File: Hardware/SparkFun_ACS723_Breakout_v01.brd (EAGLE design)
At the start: 24.1 x 15.2 mm, 19 parts, among them U1 ACS723

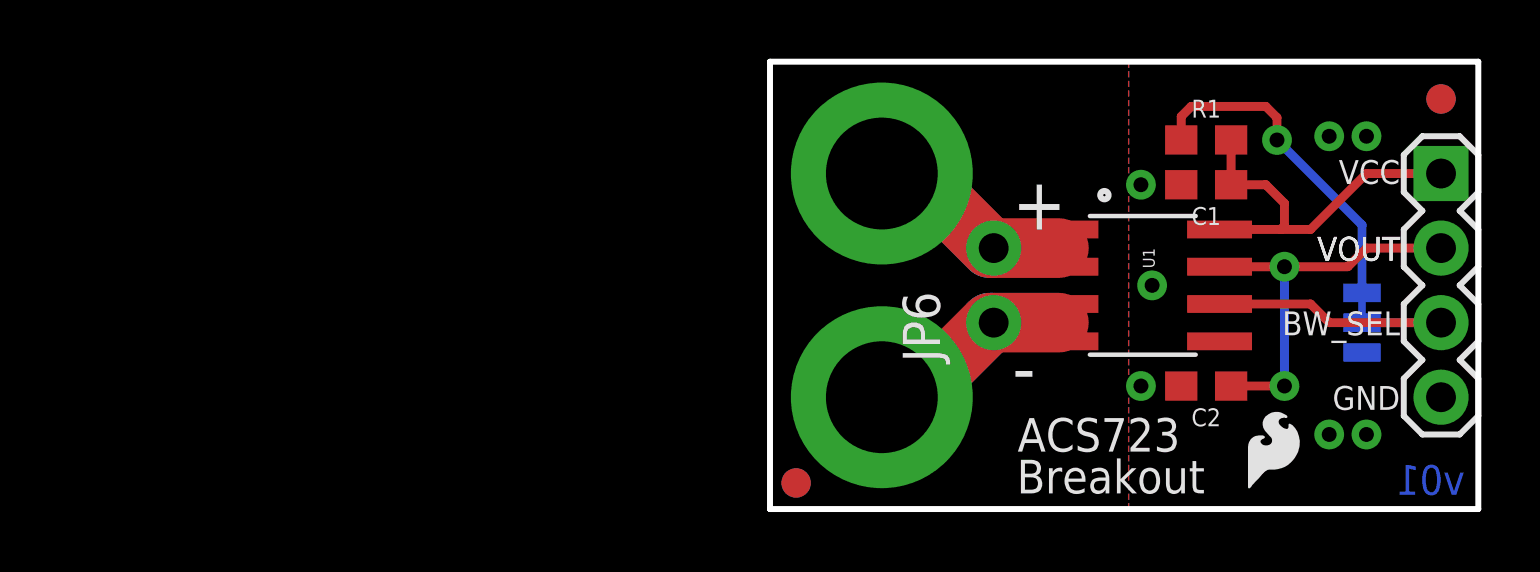
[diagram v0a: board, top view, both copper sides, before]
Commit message: finalizing v01 design
-isolated GND plane
-added 1nf decoupling cap to viout
-updated to 0603 footprints
-added bandwidth select jumper
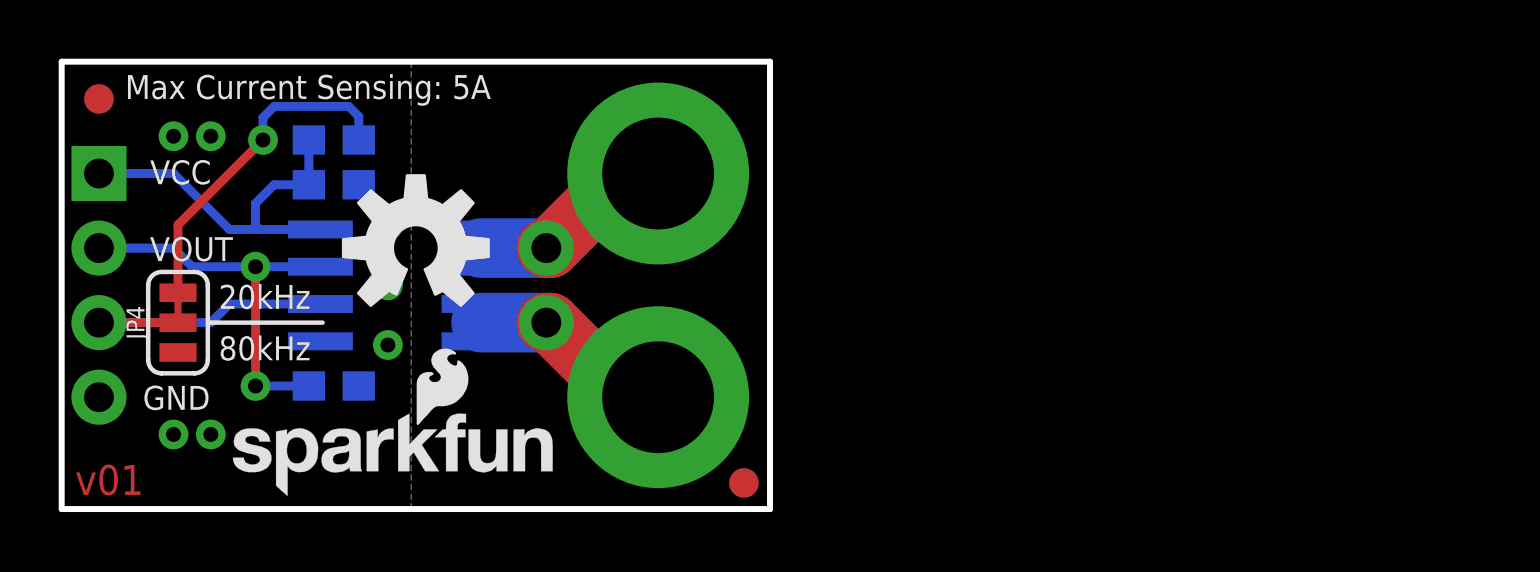
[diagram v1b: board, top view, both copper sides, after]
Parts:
- moved FD3 45.7 mm to (-22.9, 14.0), flipped to the top
- moved FD4 45.7 mm to (-22.9, 14.0), flipped to the bottom
- moved JP3 45.7 mm to (-22.9, 11.4), flipped to the bottom
- moved JP4 40.3 mm to (-20.2, 6.35), flipped to the top
- moved LOGO2 37.6 mm to (-18.8, -0.05), flipped to the top
- moved FRAME1 33.1 mm to (16.5, -11.4), flipped to the bottom
- moved U$6 32.0 mm to (-16.0, 0.38), flipped to the bottom
- moved C1 29.7 mm to (-14.9, 11.0), flipped to the bottom
- moved C2 29.7 mm to (-14.9, 4.19), flipped to the bottom
- moved R1 29.7 mm to (-14.9, 12.6), flipped to the bottom
- moved U1 25.4 mm to (-12.7, 7.62), flipped to the bottom
- moved U$5 24.6 mm to (-12.3, 2.54), flipped to the top
- moved U$3 24.1 mm to (-12.1, 8.89), flipped to the top
- moved JP6 15.2 mm to (-7.62, 6.35), flipped to the bottom
- moved U$1 10.2 mm to (5.08, -14.0), flipped to the bottom
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
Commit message: Added designer attributes
-Added "designed by" and "Revised by" attributes and frame
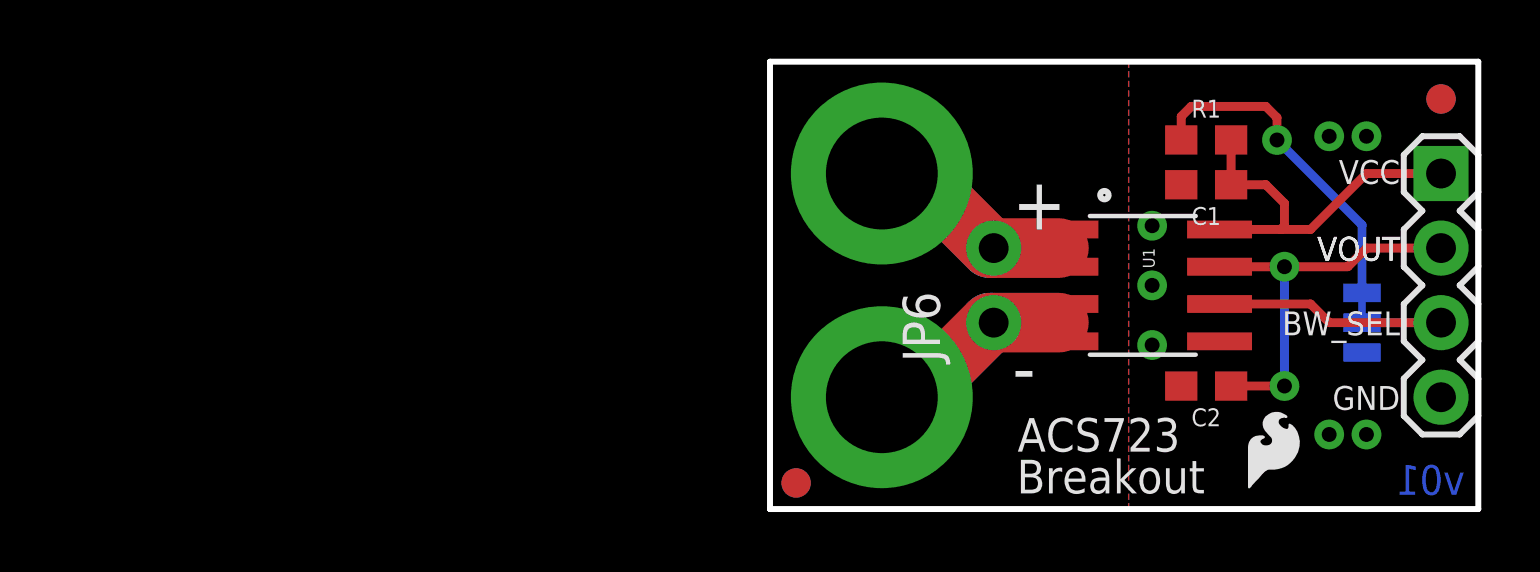
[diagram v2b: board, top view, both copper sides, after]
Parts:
- FRAME1: value (none) -> FRAME-LETTER
- U1: value ACS723 -> ACS723ACS723LLCTR-05AB-T2
- moved FD3 45.7 mm to (22.9, 14.0), flipped to the bottom
- moved FD4 45.7 mm to (22.9, 14.0), flipped to the top
- moved JP3 45.7 mm to (22.9, 11.4), flipped to the top
- moved JP4 40.3 mm to (20.2, 6.35), flipped to the bottom
- moved LOGO2 37.6 mm to (18.8, -0.05), flipped to the bottom
- moved FRAME1 33.0 mm to (-16.5, -11.4), flipped to the top
- moved U$6 32.0 mm to (16.0, 0.38), flipped to the top
- moved C1 29.7 mm to (14.9, 11.0), flipped to the top
- moved C2 29.7 mm to (14.9, 4.19), flipped to the top
- moved R1 29.7 mm to (14.9, 12.6), flipped to the top
- moved U1 25.4 mm to (12.7, 7.62), flipped to the top
- moved U$5 24.6 mm to (12.3, 2.54), flipped to the bottom
- moved U$3 24.1 mm to (12.1, 8.89), flipped to the bottom
- moved JP6 15.2 mm to (7.62, 6.35), flipped to the top
- moved U$1 10.2 mm to (-5.08, -14.0), flipped to the top
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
